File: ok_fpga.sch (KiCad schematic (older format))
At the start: 51 parts, among them J15 Conn_02x12_Counter_Clockwise, J16 Conn_Coaxial, J17 Conn_Coaxial, J18 QWIIC_CONNECTOR-1MM, U21 24AA025UID, U22 PCA9306, U23 NLSX3018DTR2G, U24 TXS0108EPW, U25 TXS0108EPW, U26 TCA9555, U27 TCA9555

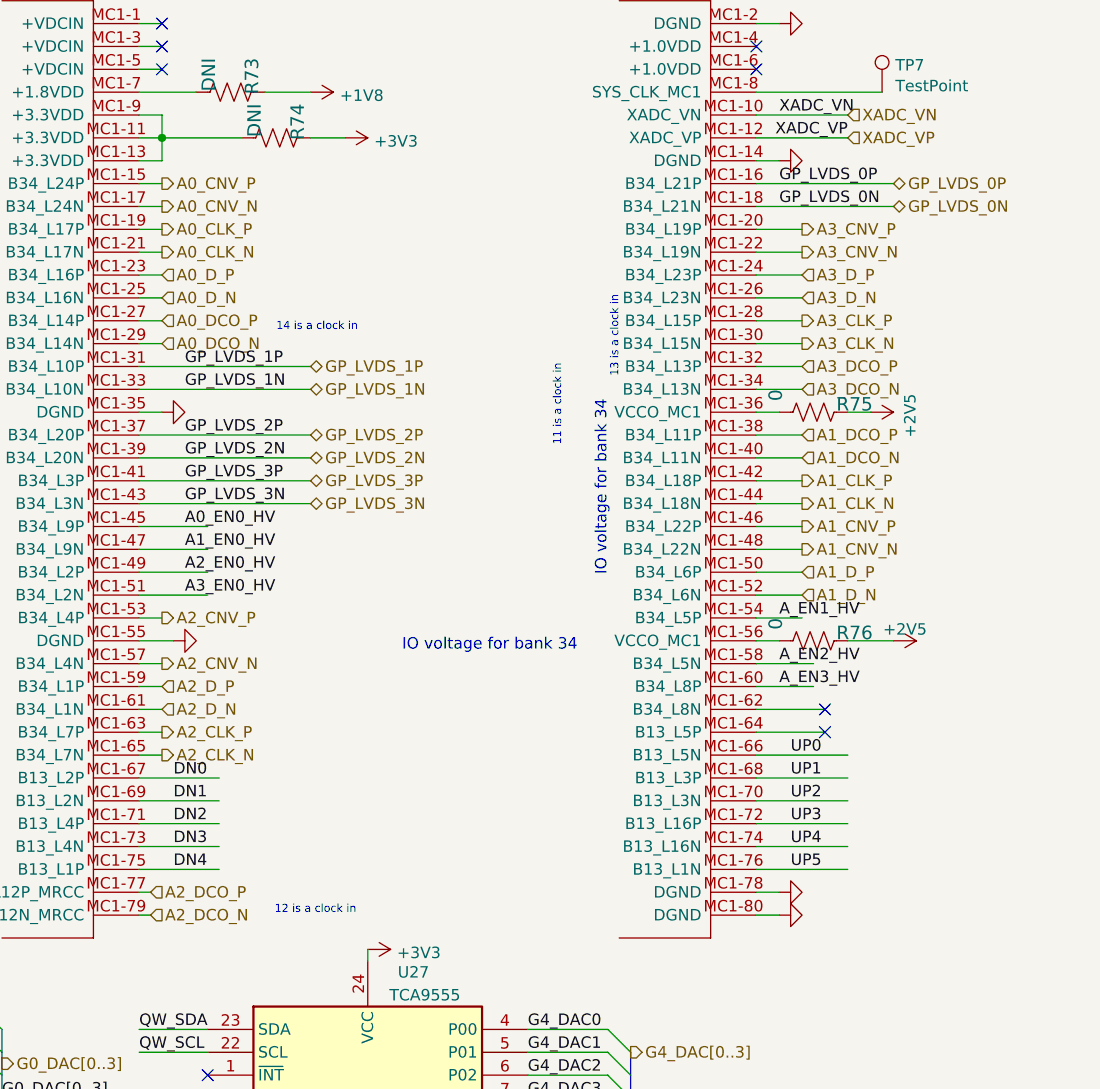
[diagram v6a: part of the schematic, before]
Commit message: moved adc pins around
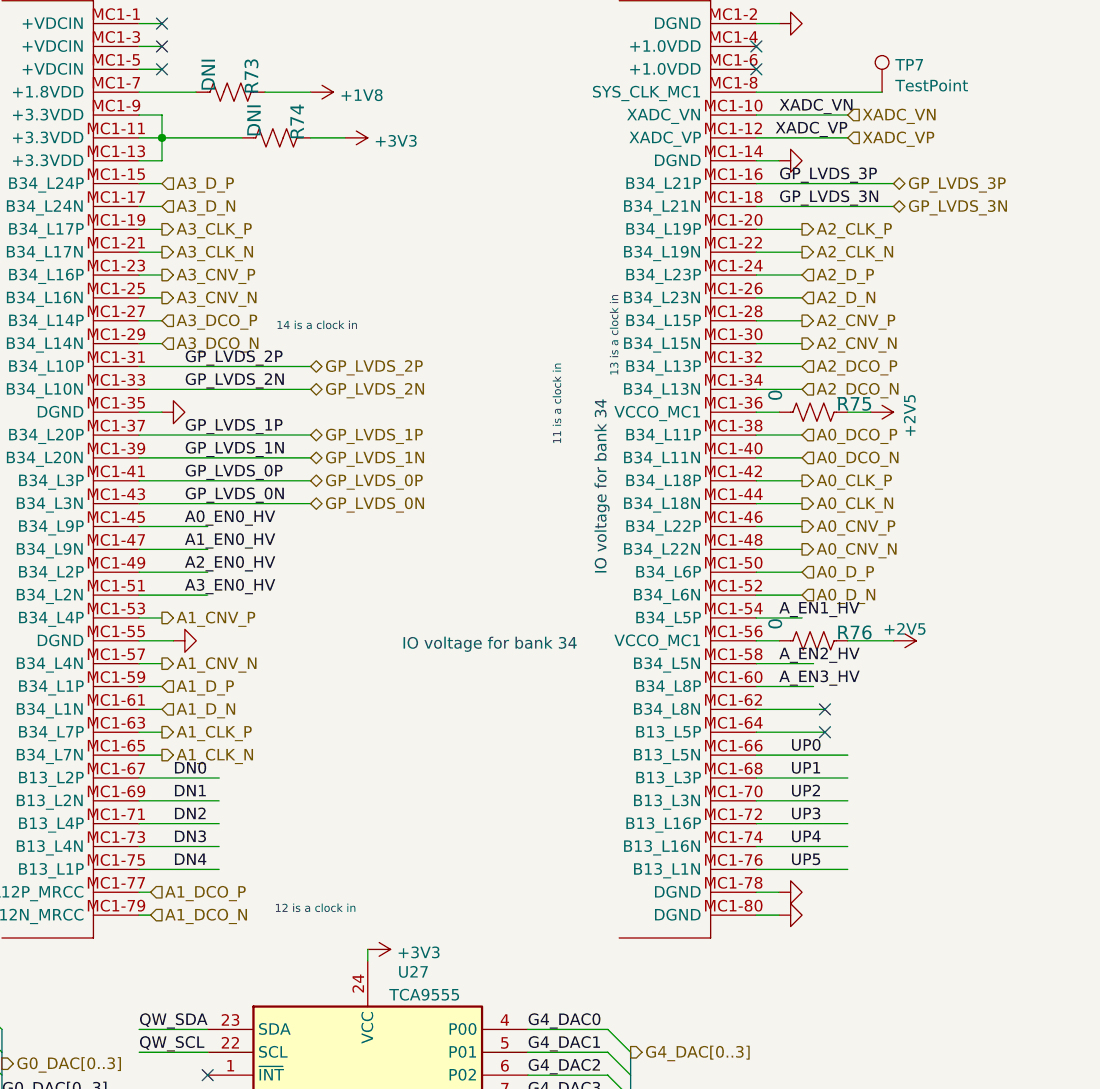
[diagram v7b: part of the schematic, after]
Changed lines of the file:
@@
 D0_SCLK
 Text HLabel 11100 3200 2    50   Input ~ 0
+A0_D_N
+Text HLabel 11100 2600 2    50   Input ~ 0
+A0_DCO_N
+Text HLabel 11100 2100 2    50   Output ~ 0
+A2_CNV_N
+Text HLabel 11100 1900 2    50   Input ~ 0
+A2_D_N
+Text HLabel 11100 2300 2    50   Input ~ 0
+A2_DCO_N
+Text HLabel 11100 3100 2    50   Input ~ 0
+A0_D_P
+Text HLabel 11100 1800 2    50   Input ~ 0
+A2_D_P
+Text HLabel 11100 2200 2    50   Input ~ 0
+A2_DCO_P
+Text HLabel 8300 3800 2    50   Output ~ 0
+A1_CLK_P
+Text HLabel 11100 2500 2    50   Input ~ 0
+A0_DCO_P
+Text HLabel 11100 2000 2    50   Output ~ 0
+A2_CNV_P
+Text HLabel 11100 3000 2    50   Output ~ 0
+A0_CNV_N
+Text HLabel 11100 2900 2    50   Output ~ 0
+A0_CNV_P
+Text HLabel 11100 2800 2    50   Output ~ 0
+A0_CLK_N
+Text HLabel 11100 1700 2    50   Output ~ 0
+A2_CLK_N
+Text HLabel 8300 3500 2    50   Output ~ 0
+A1_CNV_N
+Text HLabel 8300 3700 2    50   Input ~ 0
 A1_D_N
-Text HLabel 11100 2600 2    50   Input ~ 0
-A1_DCO_N
-Text HLabel 11100 1700 2    50   Output ~ 0
-A3_CNV_N
-Text HLabel 11100 1900 2    50   Input ~ 0
-A3_D_N
-Text HLabel 11100 2300 2    50   Input ~ 0
-A3_DCO_N
-Text HLabel 11100 3100 2    50   Input ~ 0
+Text HLabel 8300 3900 2    50   Output ~ 0
+A1_CLK_N
+Text HLabel 11100 2700 2    50   Output ~ 0
+A0_CLK_P
+Text HLabel 11100 1600 2    50   Output ~ 0
+A2_CLK_P
+Text HLabel 8300 3300 2    50   Output ~ 0
+A1_CNV_P
+Text HLabel 8300 3600 2    50   Input ~ 0
 A1_D_P
-Text HLabel 11100 1800 2    50   Input ~ 0
-A3_D_P
-Text HLabel 11100 2200 2    50   Input ~ 0
-A3_DCO_P
-Text HLabel 8300 3800 2    50   Output ~ 0
-A2_CLK_P
-Text HLabel 11100 2500 2    50   Input ~ 0
-A1_DCO_P
-Text HLabel 11100 1600 2    50   Output ~ 0
-A3_CNV_P
-Text HLabel 11100 3000 2    50   Output ~ 0
-A1_CNV_N
-Text HLabel 11100 2900 2    50   Output ~ 0
-A1_CNV_P
-Text HLabel 8300 1500 2    50   Output ~ 0
-A0_CNV_N
-Text HLabel 11100 2800 2    50   Output ~ 0
-A1_CLK_N
-Text HLabel 11100 2100 2    50   Output ~ 0
-A3_CLK_N
-Text HLabel 8300 3500 2    50   Output ~ 0
-A2_CNV_N
-Text HLabel 8300 3700 2    50   Input ~ 0
-A2_D_N
-Text HLabel 8250 4600 2    50   Input ~ 0
-A2_DCO_N
-Text HLabel 8300 3900 2    50   Output ~ 0
-A2_CLK_N
-Text HLabel 11100 2700 2    50   Output ~ 0
-A1_CLK_P
-Text HLabel 8300 1400 2    50   Output ~ 0
-A0_CNV_P
-Text HLabel 11100 2000 2    50   Output ~ 0
-A3_CLK_P
-Text HLabel 8300 3300 2    50   Output ~ 0
-A2_CNV_P
-Text HLabel 8300 1900 2    50   Input ~ 0
-A0_D_N
-Text HLabel 8300 3600 2    50   Input ~ 0
-A2_D_P
-Text HLabel 8250 4500 2    50   Input ~ 0
-A2_DCO_P
-Text HLabel 8300 1600 2    50   Output ~ 0
-A0_CLK_P
-Text HLabel 8300 1700 2    50   Output ~ 0
-A0_CLK_N
-Text HLabel 8300 1800 2    50   Input ~ 0
-A0_D_P
-Text HLabel 8300 2100 2    50   Input ~ 0
-A0_DCO_N
-Text HLabel 8300 2000 2    50   Input ~ 0
-A0_DCO_P
 Text HLabel 6350 1900 2    50   Output ~ 0
 ADS_CONVST
@@
 	1450 2850 1650 2850
 Text Label 11000 1400 0    50   ~ 0
-GP_LVDS_0P
+GP_LVDS_3P
 Text Label 11000 1500 0    50   ~ 0
-GP_LVDS_0N
+GP_LVDS_3N
 Wire Wire Line
 	8200 2300 8950 2300
@@
 	8200 2200 8950 2200
 Text Label 8400 2200 0    50   ~ 0
-GP_LVDS_1P
+GP_LVDS_2P
 Text Label 8400 2300 0    50   ~ 0
-GP_LVDS_1N
+GP_LVDS_2N
 Wire Wire Line
 	8200 2600 8950 2600
@@
 	8200 2500 8950 2500
 Text Label 8400 2500 0    50   ~ 0
-GP_LVDS_2P
+GP_LVDS_1P
 Text Label 8400 2600 0    50   ~ 0
-GP_LVDS_2N
+GP_LVDS_1N
 Wire Wire Line
 	8200 2800 8950 2800
@@
 	8200 2700 8950 2700
 Text Label 8400 2700 0    50   ~ 0
-GP_LVDS_3P
+GP_LVDS_0P
 Text Label 8400 2800 0    50   ~ 0
-GP_LVDS_3N
+GP_LVDS_0N
 Wire Wire Line
 	10900 3700 11200 3700
@@
 XADC_VP
 Text HLabel 8950 2200 2    50   BiDi ~ 0
+GP_LVDS_2P
+Text HLabel 8950 2300 2    50   BiDi ~ 0
+GP_LVDS_2N
+Text HLabel 8950 2500 2    50   BiDi ~ 0
 GP_LVDS_1P
-Text HLabel 8950 2300 2    50   BiDi ~ 0
+Text HLabel 8950 2600 2    50   BiDi ~ 0
 GP_LVDS_1N
-Text HLabel 8950 2500 2    50   BiDi ~ 0
-GP_LVDS_2P
-Text HLabel 8950 2600 2    50   BiDi ~ 0
-GP_LVDS_2N
 Text HLabel 8950 2700 2    50   BiDi ~ 0
+GP_LVDS_0P
+Text HLabel 8950 2800 2    50   BiDi ~ 0
+GP_LVDS_0N
+Text HLabel 11500 1400 2    50   BiDi ~ 0
 GP_LVDS_3P
-Text HLabel 8950 2800 2    50   BiDi ~ 0
+Text HLabel 11500 1500 2    50   BiDi ~ 0
 GP_LVDS_3N
-Text HLabel 11500 1400 2    50   BiDi ~ 0
-GP_LVDS_0P
-Text HLabel 11500 1500 2    50   BiDi ~ 0
-GP_LVDS_0N
 $Comp
 L Device:R_Small_US R288
@@
 Text Label 1500 1850 0    50   ~ 0
 1V8_SDA
+Text HLabel 8300 2100 2    50   Input ~ 0
+A3_DCO_N
+Text HLabel 8300 2000 2    50   Input ~ 0
+A3_DCO_P
+Text HLabel 8300 1500 2    50   Input ~ 0
+A3_D_N
+Text HLabel 8300 1400 2    50   Input ~ 0
+A3_D_P
+Text HLabel 8300 1700 2    50   Output ~ 0
+A3_CLK_N
+Text HLabel 8300 1600 2    50   Output ~ 0
+A3_CLK_P
+Text HLabel 8300 1900 2    50   Output ~ 0
+A3_CNV_N
+Text HLabel 8300 1800 2    50   Output ~ 0
+A3_CNV_P
+Text HLabel 8250 4600 2    50   Input ~ 0
+A1_DCO_N
+Text HLabel 8250 4500 2    50   Input ~ 0
+A1_DCO_P
 Wire Bus Line
 	7600 5500 7600 5800

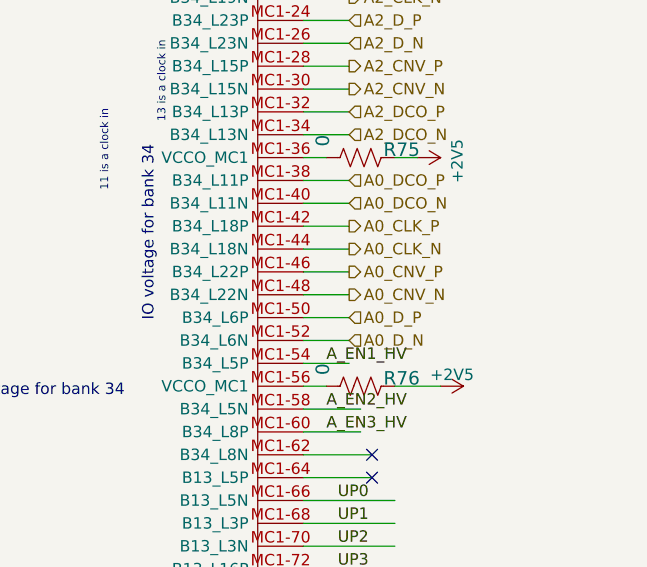
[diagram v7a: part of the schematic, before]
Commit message: updates after bug in ADS8686 power connectivity. And swap of DC SCL and SDA
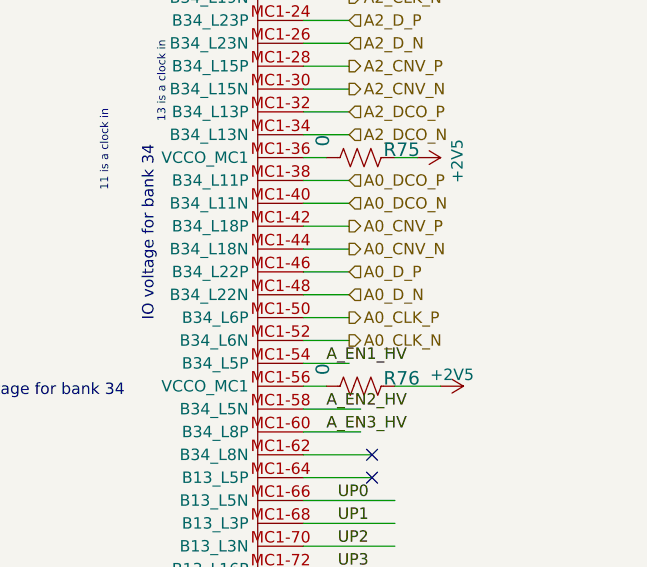
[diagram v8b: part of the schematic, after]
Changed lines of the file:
@@
 Text HLabel 3000 2900 2    50   Output ~ 0
 D0_SCLK
-Text HLabel 11100 3200 2    50   Input ~ 0
+Text HLabel 11100 3000 2    50   Input ~ 0
 A0_D_N
 Text HLabel 11100 2600 2    50   Input ~ 0
@@
 Text HLabel 11100 2300 2    50   Input ~ 0
 A2_DCO_N
-Text HLabel 11100 3100 2    50   Input ~ 0
+Text HLabel 11100 2900 2    50   Input ~ 0
 A0_D_P
 Text HLabel 11100 1800 2    50   Input ~ 0
@@
 Text HLabel 11100 2000 2    50   Output ~ 0
 A2_CNV_P
-Text HLabel 11100 3000 2    50   Output ~ 0
+Text HLabel 11100 2800 2    50   Output ~ 0
 A0_CNV_N
-Text HLabel 11100 2900 2    50   Output ~ 0
+Text HLabel 11100 2700 2    50   Output ~ 0
 A0_CNV_P
-Text HLabel 11100 2800 2    50   Output ~ 0
+Text HLabel 11100 3200 2    50   Output ~ 0
 A0_CLK_N
 Text HLabel 11100 1700 2    50   Output ~ 0
@@
 Text HLabel 8300 3900 2    50   Output ~ 0
 A1_CLK_N
-Text HLabel 11100 2700 2    50   Output ~ 0
+Text HLabel 11100 3100 2    50   Output ~ 0
 A0_CLK_P
 Text HLabel 11100 1600 2    50   Output ~ 0
